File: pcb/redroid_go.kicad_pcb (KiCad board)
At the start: 2 copper layers, 70 x 95 mm, 100 parts, among them J1 USB4105-GF-A, J2 5051101892, J3 Conn_01x02_Pin, J4 Conn_01x10_Pin, Q1 UMH3N, Q2 PMOS, Q3 UMH3N, SW1 UP, SW10 A, SW11 SW_SPDT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

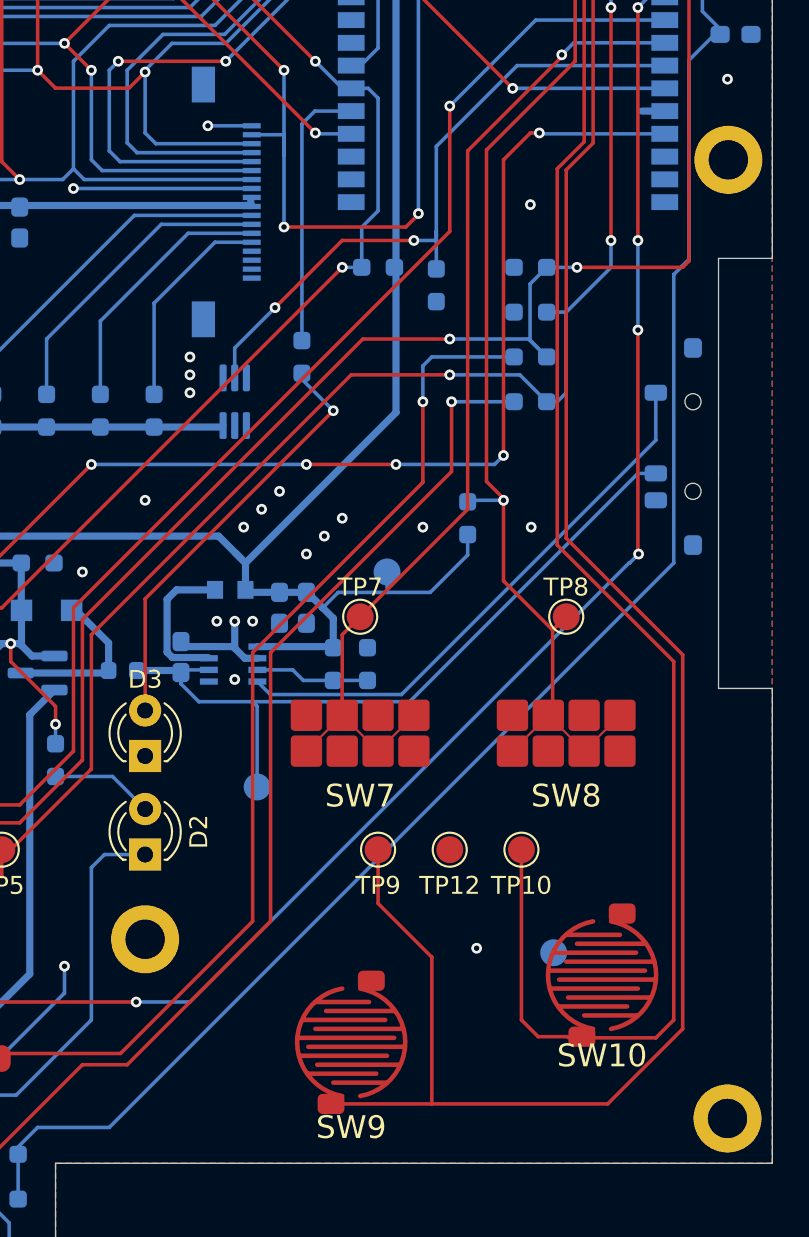
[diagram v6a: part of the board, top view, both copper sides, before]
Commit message: Fix switch hole size
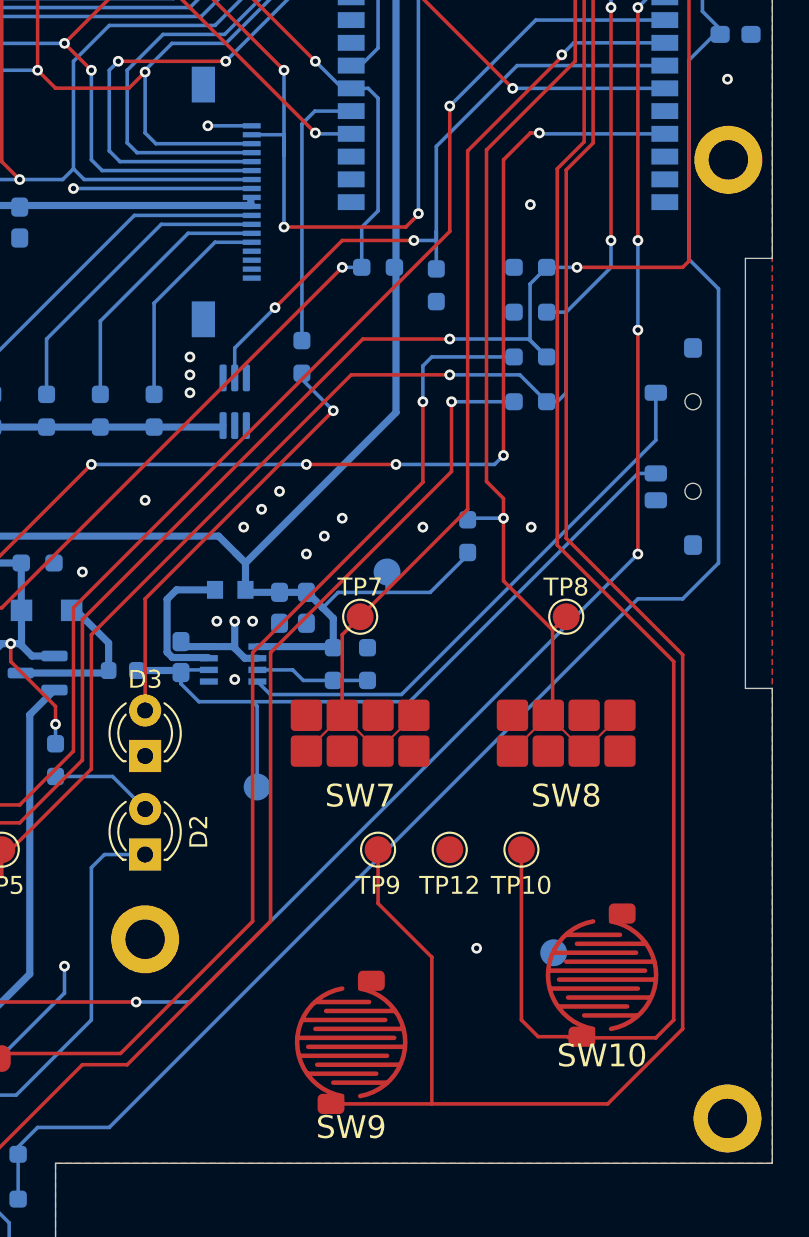
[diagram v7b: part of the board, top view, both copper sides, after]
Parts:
- moved R15 1.00 mm to (181.5, 93.5)
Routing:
- net IO36: track 95.1 -> 97.9 mm
- net GND: track 73.8 -> 72.6 mm
- net P3V3: track 271.6 -> 270.4 mm
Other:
- outline, holes or cut-outs redrawn
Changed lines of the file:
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@@
 	(footprint "Resistor_SMD:R_0603_1608Metric_Pad0.98x0.95mm_HandSolder"
 		(layer "B.Cu")
-		(at 181.5 92.5 -90)
+		(at 181.5 93.5 -90)
 		(descr "Resistor SMD 0603 (1608 Metric), square (rectangular) end terminal, IPC_7351 nominal with elongated pad for handsoldering. (Body size source: IPC-SM-782 page 72, https://www.pcb-3d.com/wordpress/wp-content/uploads/ipc-sm-782a_amendment_1_and_2.pdf), generated with kicad-footprint-generator")
 		(tags "resistor handsolder")
@@
 	)
 	(gr_line
-		(start 195.5 78)
+		(start 197 78)
 		(end 198.5 78)
 		(stroke
@@
 	)
 	(gr_line
-		(start 195.5 90)
-		(end 195.5 102)
+		(start 197 90)
+		(end 197 102)
 		(stroke
 			(width 0.05)
@@
 	)
 	(gr_line
-		(start 195.5 102)
+		(start 197 102)
 		(end 198.5 102)
 		(stroke
@@
 	)
 	(gr_line
-		(start 195.5 90)
-		(end 195.5 78)
+		(start 197 90)
+		(end 197 78)
 		(stroke
 			(width 0.05)
@@
 	)
 	(segment
-		(start 192.5 69.78)
-		(end 191.22 69.78)
-		(width 0.4)
-		(layer "B.Cu")
-		(net 1)
-	)
-	(segment
 		(start 135.075001 124.675)
 		(end 134.5 124.099999)
@@
 	)
 	(segment
-		(start 181.5 94.550898)
-		(end 181.5 93.4125)
-		(width 0.2)
-		(layer "B.Cu")
-		(net 3)
-	)
-	(segment
 		(start 167.45 56.95)
 		(end 167.4 57)
@@
 	)
 	(segment
-		(start 191 94.461992)
-		(end 191 82)
-		(width 0.2)
-		(layer "F.Cu")
-		(net 7)
-	)
-	(segment
-		(start 191.038008 94.5)
-		(end 191 94.461992)
+		(start 191 64)
+		(end 191 77)
 		(width 0.2)
 		(layer "F.Cu")
@@
 	)
 	(segment
-		(start 191 64)
-		(end 191 77)
+		(start 191 94.5)
+		(end 191 82)
 		(width 0.2)
 		(layer "F.Cu")
@@
 	)
 	(via
-		(at 191.038008 94.5)
+		(at 191 94.5)
 		(size 0.6)
 		(drill 0.3)
@@
 	)
 	(segment
+		(start 166 119.5)
+		(end 163 119.5)
+		(width 0.2)
+		(layer "B.Cu")
+		(net 7)
+	)
+	(segment
 		(start 142.0875 120.725)
 		(end 143 121.6375)
@@
 	)
 	(segment
-		(start 190.538008 95)
-		(end 190.5 95)
+		(start 134 124.5)
+		(end 134 121.5)
 		(width 0.2)
 		(layer "B.Cu")
@@
 	)
 	(segment
-		(start 134 124.5)
-		(end 134 121.5)
+		(start 191 94.5)
+		(end 166 119.5)
 		(width 0.2)
 		(layer "B.Cu")
@@
 	)
 	(segment
-		(start 190.5 95)
-		(end 166 119.5)
-		(width 0.2)
-		(layer "B.Cu")
-		(net 7)
-	)
-	(segment
-		(start 166 119.5)
-		(end 163 119.5)
-		(width 0.2)
-		(layer "B.Cu")
-		(net 7)
-	)
-	(segment
 		(start 191.57 63.43)
 		(end 191 64)
@@
 	)
 	(segment
-		(start 191.038008 94.5)
-		(end 190.538008 95)
-		(width 0.2)
-		(layer "B.Cu")
-		(net 7)
-	)
-	(segment
 		(start 134.775 120.725)
 		(end 142.0875 120.725)
@@
 	)
 	(segment
-		(start 161.5 126.5)
-		(end 157.5 126.5)
+		(start 156.4125 127.5875)
+		(end 156.4125 128)
 		(width 0.2)
 		(layer "B.Cu")
@@
 	)
 	(segment
-		(start 156.4125 128)
-		(end 156.4125 130.5)
+		(start 195.5 95)
+		(end 193.5 97)
 		(width 0.2)
 		(layer "B.Cu")
@@
 	)
 	(segment
-		(start 192.5 55.81)
-		(end 193.4493 55.81)
+		(start 156.4125 128)
+		(end 156.4125 130.5)
 		(width 0.2)
 		(layer "B.Cu")
@@
 	)
 	(segment
-		(start 193 78.901304)
-		(end 193 95)
+		(start 193.4493 55.81)
+		(end 194.6 56.9607)
 		(width 0.2)
 		(layer "B.Cu")
@@
 	)
 	(segment
-		(start 193.85 66.9375)
-		(end 193.85 78.051304)
+		(start 191 97)
+		(end 161.5 126.5)
 		(width 0.2)
 		(layer "B.Cu")
@@
 	)
 	(segment
-		(start 193 95)
-		(end 161.5 126.5)
+		(start 193.5 97)
+		(end 191 97)
 		(width 0.2)
 		(layer "B.Cu")
@@
 	)
 	(segment
-		(start 194.6 64.2125)
-		(end 195.5875 65.2)
+		(start 193.85 66.9375)
+		(end 193.85 78.051304)
 		(width 0.2)
 		(layer "B.Cu")
@@
 	)
 	(segment
-		(start 193.4493 55.81)
-		(end 194.6 56.9607)
+		(start 161.5 126.5)
+		(end 157.5 126.5)
+		(width 0.2)
+		(layer "B.Cu")
+		(net 13)
+	)
+	(segment
+		(start 192.5 55.81)
+		(end 193.4493 55.81)
+		(width 0.2)
+		(layer "B.Cu")
+		(net 13)
+	)
+	(segment
+		(start 194.6 64.2125)
+		(end 195.5875 65.2)
 		(width 0.2)
 		(layer "B.Cu")
@@
 	(segment
 		(start 193.85 78.051304)
-		(end 193 78.901304)
+		(end 195.5 79.701304)
 		(width 0.2)
 		(layer "B.Cu")
@@
 	)
 	(segment
-		(start 156.4125 127.5875)
-		(end 156.4125 128)
+		(start 195.5 79.701304)
+		(end 195.5 95)
 		(width 0.2)
 		(layer "B.Cu")
@@
 	)
 	(segment
-		(start 183.5 91.5)
-		(end 183.5 96)
+		(start 183.5 91.4)
+		(end 182.55 90.45)
 		(width 0.2)
 		(layer "F.Cu")
@@
 	)
 	(segment
-		(start 182.55 90.45)
-		(end 182.55 71.95)
+		(start 186.98452 98)
+		(end 186.24226 98.74226)
+		(width 0.2)
+		(layer "F.Cu")
+		(net 59)
+	)
+	(segment
+		(start 182.55 71.95)
+		(end 187.5 67)
 		(width 0.2)
 		(layer "F.Cu")
@@
 	)
 	(segment
-		(start 186.98452 98)
+		(start 183.5 96)
 		(end 186.24226 98.74226)
 		(width 0.2)
@@
 	)
 	(segment
-		(start 183.5 91.5)
-		(end 183.5 91.4)
+		(start 187.5 61)
+		(end 191 57.5)
 		(width 0.2)
 		(layer "F.Cu")
@@
 	)
 	(segment
-		(start 182.55 71.95)
-		(end 187.5 67)
+		(start 183.5 92.5)
+		(end 183.5 96)
 		(width 0.2)
 		(layer "F.Cu")
@@
 	)
 	(segment
-		(start 183.5 91.4)
-		(end 182.55 90.45)
-		(width 0.2)
-		(layer "F.Cu")
-		(net 59)
-	)
-	(segment
-		(start 183.5 96)
-		(end 186.24226 98.74226)
+		(start 182.55 90.45)
+		(end 182.55 71.95)
 		(width 0.2)
 		(layer "F.Cu")
@@
 	)
 	(segment
-		(start 187.5 61)
-		(end 191 57.5)
+		(start 183.5 92.5)
+		(end 183.5 91.4)
 		(width 0.2)
 		(layer "F.Cu")
@@
 	)
 	(via
-		(at 183.5 91.5)
+		(at 183.5 92.5)
 		(size 0.6)
 		(drill 0.3)
@@
 	)
 	(segment
-		(start 181.5 91.5875)
-		(end 181.5875 91.5)
+		(start 183.5 92.5)
+		(end 181.5875 92.5)
 		(width 0.2)
 		(layer "B.Cu")
@@
 		(width 0.2)
 		(layer "B.Cu")
-		(net 59)
-	)
-	(segment
-		(start 181.5875 91.5)
-		(end 183.5 91.5)
-		(width 0.2)
-		(layer "B.Cu")
